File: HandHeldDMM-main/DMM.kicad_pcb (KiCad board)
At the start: 2 copper layers, 60 x 100 mm, 149 parts, among them IC1 REF35300QDBVR, J1 Conn_02x03_Odd_Even, J2 Conn_01x02, J3 Conn_01x03, J4 Conn_02x05_Odd_Even, J5 Conn_01x02, J6 Conn_01x04, J7 Conn_01x02, J8 Conn_01x01, J9 Conn_01x01, Q1 HD6362, Q10 SI2301, Q11 SI2301, Q12 SI2301, Q2 HD6362, Q3 SI2302, Q4 SI2302, Q5 SI2302, Q6 SI2301, Q7 SI2301, Q8 HD6362, Q9 SI2301, SW1 SW_Push, SW2 SW_Push, SW3 SW_Push, SW4 SW_Push, U1 TLP291, U10 TLP291, U11 LM334M, U15 CPC1017N, U17 TLP291, U18 TLP291, U19 TLP291, U20 TLP291, U21 TLP291, U22 CPC1017N, U23 CPC1017N, U24 AMS1117-5.0, U26 TL7660CDR, U27 TL7660CDR, U28 TL7660CDR, U29 CPC1017N, U3 TLP291, U30 CPC1017N, U31 CPC1017N, U4 TLP291, U5 OPA2140, U6 TLP291, U7 STM32F373CCTx, U8 AMS1117-3.3, U9 TLP291, Y1 16Mhz

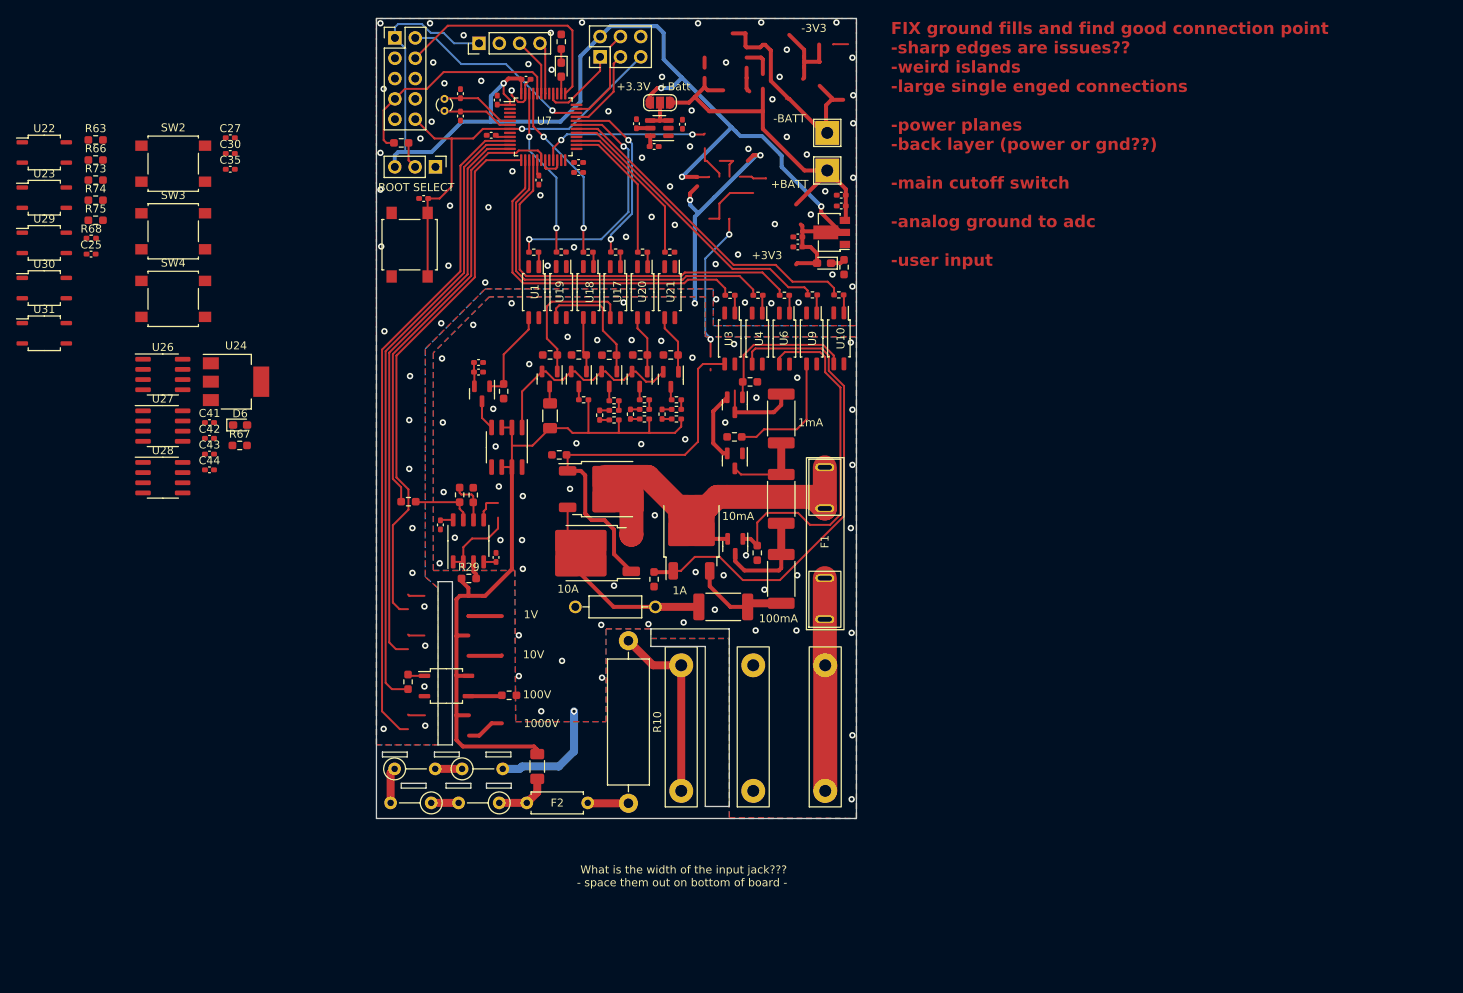
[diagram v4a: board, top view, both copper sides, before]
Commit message: Layout / routing V2 with schematic fixes
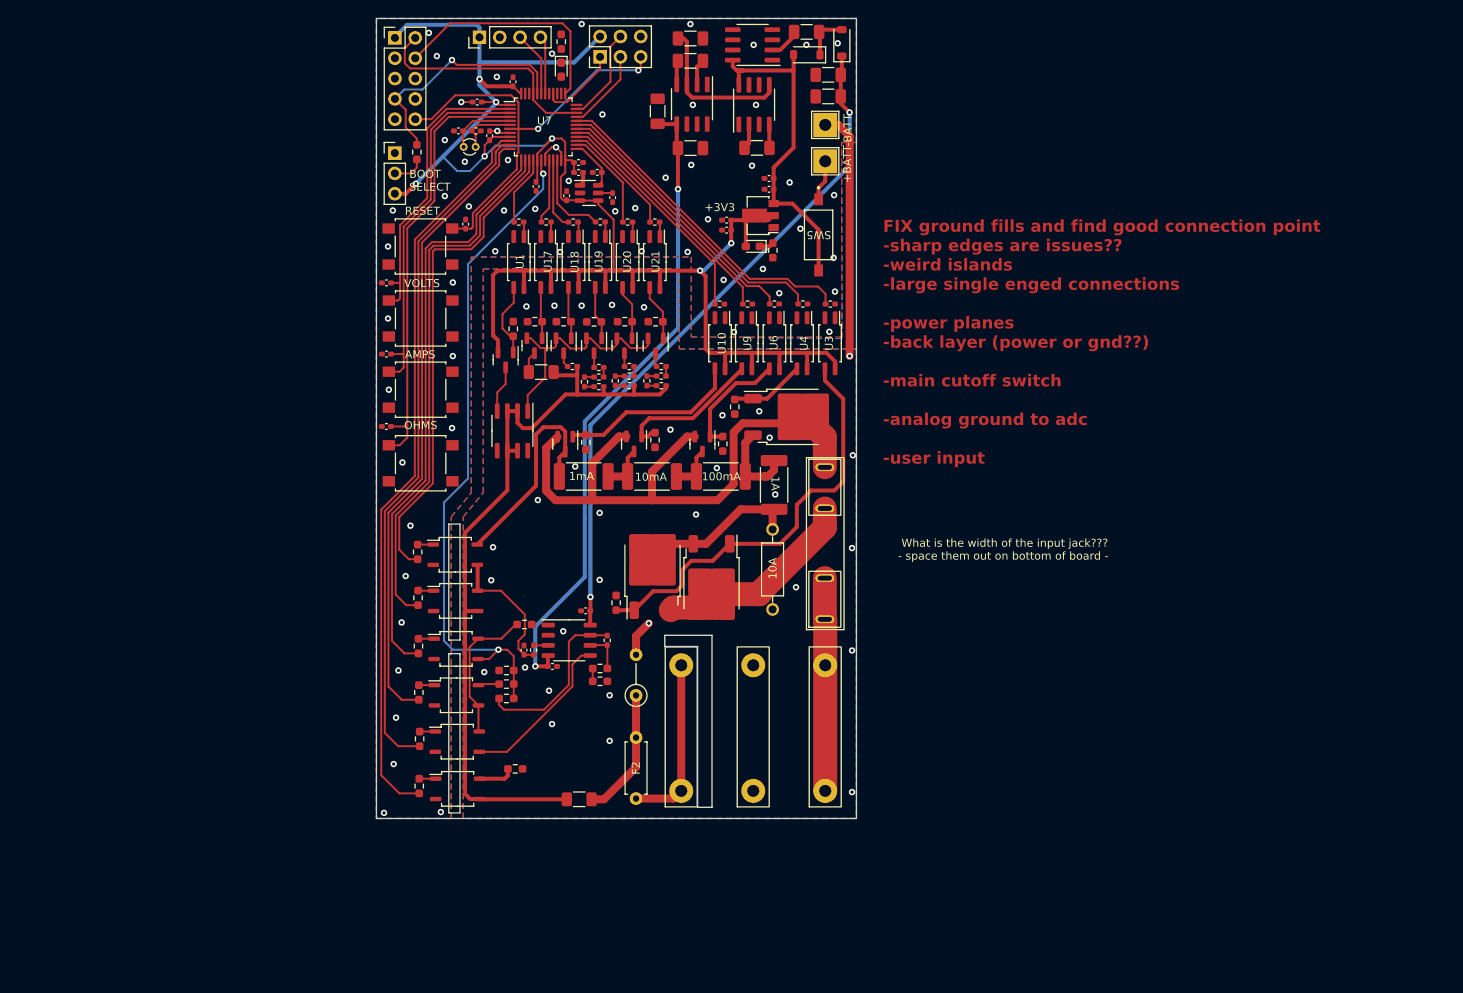
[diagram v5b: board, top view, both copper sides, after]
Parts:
- removed C41, C44: 1uF, Capacitor_SMD:C_0402_1005Metric_Pad0.74x0.62mm_HandSolder
- removed C42, C43: 100nF, Capacitor_SMD:C_0402_1005Metric_Pad0.74x0.62mm_HandSolder
- removed D6: LED, LED_SMD:LED_0603_1608Metric_Pad1.05x0.95mm_HandSolder
- removed JP1: Jumper_3_Open, Jumper:SolderJumper-3_P1.3mm_Open_RoundedPad1.0x1.5mm_NumberLabels
- removed R10: 1K, Resistor_THT:R_Axial_DIN0516_L15.5mm_D5.0mm_P20.32mm_Horizontal
- removed R67: 1k, Resistor_SMD:R_0603_1608Metric_Pad0.98x0.95mm_HandSolder
- removed RV2, RV3, RV4: Varistor, Resistor_THT:R_Axial_DIN0207_L6.3mm_D2.5mm_P5.08mm_Vertical
- removed U24: AMS1117-5.0, Package_TO_SOT_SMD:SOT-223-3_TabPin2
- added C13: 10uF, Capacitor_SMD:C_1206_3216Metric_Pad1.33x1.80mm_HandSolder, F.Cu at (168.3, 39.3)
- added C14: 10uF, Capacitor_SMD:C_1206_3216Metric_Pad1.33x1.80mm_HandSolder, F.Cu at (172.4, 33.0)
- added C15: DNP, Capacitor_SMD:C_1206_3216Metric_Pad1.33x1.80mm_HandSolder, F.Cu at (172.4, 43.9)
- added C17: 10uF, Capacitor_SMD:C_1206_3216Metric_Pad1.33x1.80mm_HandSolder, F.Cu at (172.4, 30.2)
- added C38: 10uF, Capacitor_SMD:C_1206_3216Metric_Pad1.33x1.80mm_HandSolder, F.Cu at (186.9, 29.4)
- added C40: DNP, Capacitor_SMD:C_1206_3216Metric_Pad1.33x1.80mm_HandSolder, F.Cu at (189.6, 37.4)
- added D1: 1N4148W, Diode_SMD:D_SOD-123, F.Cu at (191.3, 30.7)
- added D4: 1N4148W, Diode_SMD:D_SOD-123, F.Cu at (186.9, 32.2)
- added R1: 1K, Resistor_SMD:R_0603_1608Metric_Pad0.98x0.95mm_HandSolder, F.Cu at (161.1, 110.5)
- added R69: 4K, Resistor_SMD:R_0603_1608Metric_Pad0.98x0.95mm_HandSolder, F.Cu at (149.4, 110.9)
- added R70: 1K, Resistor_SMD:R_0603_1608Metric_Pad0.98x0.95mm_HandSolder, F.Cu at (149.4, 109.2)
- added SW5: SW_SPST, Custom Lib:Dip Switch, F.Cu at (188.4, 54.2)
- C11: value 100nF -> 10uF; footprint Capacitor_SMD:C_0402_1005Metric_Pad0.74x0.62mm_HandSolder -> Capacitor_SMD:C_1206_3216Metric_Pad1.33x1.80mm_HandSolder
- C12: value 1uF -> 10uF; footprint Capacitor_SMD:C_0402_1005Metric_Pad0.74x0.62mm_HandSolder -> Capacitor_SMD:C_1206_3216Metric_Pad1.33x1.80mm_HandSolder
- R15: value 10K -> 1K
- R16: value 145K -> 18K; footprint Resistor_SMD:R_0603_1608Metric_Pad0.98x0.95mm_HandSolder -> Resistor_SMD:R_0402_1005Metric_Pad0.72x0.64mm_HandSolder
- R30, R9: value 1k -> 1K
- moved U28 91.4 mm to (180.2, 31.0), turned to 180 degrees
- moved U27 84.1 mm to (180.4, 38.5), turned to 90 degrees
- moved R75 76.4 mm to (138.6, 117.8), turned to 90 degrees
- moved U22 76.1 mm to (143.1, 100.5)
- moved R68 75.6 mm to (152.8, 106.7), turned to 90 degrees
- moved U26 74.3 mm to (172.6, 38.4), turned to -90 degrees
- moved R74 73.6 mm to (138.4, 112.0), turned to 90 degrees
- moved C25 73.3 mm to (151.6, 106.7), turned to 90 degrees
- moved U31 72.6 mm to (143.2, 118.1)
- moved U30 72.4 mm to (143.2, 112.3)
- moved U29 72.3 mm to (143.1, 106.5)
- moved R73 70.9 mm to (138.4, 106.2), turned to 90 degrees
- moved R63 70.0 mm to (138.3, 100.1), turned to 90 degrees
- moved U23 68.0 mm to (143.0, 94.7)
- moved R66 63.4 mm to (138.3, 94.4), turned to 90 degrees
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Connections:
- net GPIO_14 renamed OOpto5
- net GPIO_15 renamed OOpto6
- net GPIO_8 renamed AOpto4
- net RButton renamed OButton
- C11 pad 1: +3.3V -> Net-(U27-CAP-)
- C11 pad 2: GNDA -> Net-(U27-CAP+)
- C12 pad 1: +3.3V -> GND
- C12 pad 2: GNDA -> OpAmpSupply+
- C25 pad 2: GNDA -> GND
- C6 pad 2: GNDA -> GND
- C7 pad 1: GNDA -> GND
- C8 pad 1: Net-(IC1-EN) -> +3.3V
- F2 pad 1: Net-(F2-Pad1) -> InputPosRaw
- IC1 pad 3: Net-(IC1-EN) -> +3.3V
- IC1 pad 4: Net-(IC1-EN) -> +3.3V
- J5 pad 1: GNDA -> GND
- J5 pad 2: GNDA -> GND
- J8 pad 1: +9V -> Net-(J8-Pin_1)
- R11 pad 1: GPIO_10 -> OOpto1
- R15 pad 1: GNDA -> Net-(R1-Pad2)
- R2 pad 2: GNDA -> GND
- R20 pad 1: GNDA -> GND
- R21 pad 2: GNDA -> GND
- R25 pad 1: GPIO_2 -> VOpto1
- R31 pad 2: GNDA -> GND
- R33 pad 2: GNDA -> GND
- R34 pad 2: GNDA -> GND
- R35 pad 2: GNDA -> GND
- R4 pad 1: GPIO_5 -> AOpto1
- R5 pad 2: GPIO_6 -> AOpto2
- R50 pad 1: GNDA -> GND
- R51 pad 1: GNDA -> GND
- R52 pad 2: GPIO_11 -> OOpto2
- R53 pad 1: GNDA -> GND
- R54 pad 2: GNDA -> GND
- R55 pad 2: GPIO_12 -> OOpto3
- R56 pad 1: GNDA -> GND
- R58 pad 2: GPIO_13 -> OOpto4
- R59 pad 1: GNDA -> GND
- R6 pad 2: GPIO_7 -> AOpto3
- R63 pad 1: GPIO_3 -> ADCOpto2
- R66 pad 1: GPIO_4 -> ADCOpto1
- R73 pad 1: GPIO_5 -> ADCOpto3
- R74 pad 1: GPIO_4 -> ADCOpto4
- R75 pad 1: GPIO_4 -> ADCOpto5
- R8 pad 2: GPIO_9 -> AOpto5
- RV1 pad 2: Net-(RV1-Pad2) -> GND
- U15 pad 3: Net-(R54-Pad1) -> InputPos
- U15 pad 4: InputPos -> Net-(R54-Pad1)
- U22 pad 3: OpAmpIn -> InputPos
- U22 pad 4: InputPos -> OpAmpIn
- U23 pad 3: CurrentOut -> OpAmpIn
- U23 pad 4: OpAmpIn -> CurrentOut
- U28 pad 8: Net-(D4-A) -> +9V
- U30 pad 3: Net-(R69-Pad1) -> BufferOut
- U30 pad 4: BufferOut -> Net-(R69-Pad1)
- U7 pad 10: GPIO_1 -> VOpto1
- U7 pad 11: GPIO_2 -> ADCOpto5
- U7 pad 12: GPIO_3 -> ADCOpto4
- U7 pad 13: GPIO_4 -> ADCOpto3
- U7 pad 14: GPIO_5 -> ADCOpto2
- U7 pad 15: GPIO_6 -> ADCOpto1
- U7 pad 16: GPIO_7 -> OOpto1
- U7 pad 19: GNDA -> GND
- U7 pad 20: unconnected-(U7-PB2-Pad20) -> OOpto2
- U7 pad 21: SD-ADC2 -> OOpto3
- U7 pad 22: GNDA -> OOpto4
- U7 pad 28: unconnected-(U7-PD8-Pad28) -> AOpto5
- U7 pad 30: GPIO_9 -> AOpto3
- U7 pad 31: GPIO_10 -> AOpto2
- U7 pad 32: GPIO_11 -> AOpto1
- U7 pad 39: GPIO_17 -> unconnected-(U7-PB3-Pad39)
- U7 pad 41: GPIO_16 -> unconnected-(U7-PB5-Pad41)
- U7 pad 45: GPIO_12 -> SWDIOPassThrough
- U7 pad 46: GPIO_13 -> unconnected-(U7-PB9-Pad46)
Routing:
- net VOpto1: track 0.00 -> 92.3 mm
- net ADCOpto5: track 0.00 -> 85.8 mm
- net GPIO_1: track 83.9 -> 0.00 mm
- net OpAmpSupply+: track 1.62 -> 85.1 mm, vias 0 -> 2
- net OpAmpSupply-: track 1.55 -> 80.6 mm, vias 0 -> 2
- net (no net): track 78.8 -> 0.00 mm, vias 2 -> 0
- net GPIO_2: track 78.5 -> 0.00 mm
- net ADCOpto4: track 0.00 -> 78.4 mm
- net ADCOpto3: track 0.00 -> 73.4 mm
- net GPIO_3: track 72.3 -> 0.00 mm
- net GPIO_4: track 68.0 -> 0.00 mm
- net ADCOpto2: track 0.00 -> 67.0 mm
- net ADCOpto1: track 0.00 -> 60.9 mm
- net +3.3V: track 164.0 -> 223.4 mm, vias 4 -> 7
- net OButton: track 0.00 -> 54.6 mm
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- removed copper zone on B.Cu, net GNDA
- removed copper zone on F.Cu, net GNDA
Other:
- outline, holes or cut-outs redrawn
- board text added: "AMPS"
- board text added: "OHMS"
- board text added: "RESET"
- board text added: "VOLTS"
- board text removed: "+3.3V"
- board text removed: "+Batt"
- board text removed: "-3V3"
- board text removed: "1000V"
- board text removed: "100V"
- board text removed: "10V"
- board text removed: "1V"

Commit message: Finished?
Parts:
- moved C26 14.7 mm to (149.0, 35.6), turned to 90 degrees
- moved R56 1.79 mm to (165.8, 64.8), turned to -90 degrees
- moved R53 1.75 mm to (161.9, 64.8), turned to -90 degrees
- moved R59 1.71 mm to (169.5, 64.7), turned to -90 degrees
- moved R51 1.56 mm to (157.9, 64.8), turned to -90 degrees
- moved C25 1.15 mm to (151.7, 107.8), turned to -90 degrees
- moved IC1 0.40 mm to (159.8, 49.9)
- moved C8 0.40 mm to (157.0, 50.2)
- moved C10 0.31 mm to (162.7, 50.4)
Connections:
- U7 pad 45: SWDIOPassThrough -> SWDIO
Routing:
- net GND: track 45.9 -> 65.3 mm, vias 91 -> 99
- net InputAmps: track 96.4 -> 101.6 mm
- net Net-(Q1-G): track 52.9 -> 49.5 mm, vias 0 -> 2
- net Net-(U5A--): track 0.00 -> 3.36 mm
- net GPIO_LED: track 0.00 -> 2.11 mm
- net Net-(R5-Pad1): track 0.00 -> 1.75 mm
- net Net-(R6-Pad1): track 0.00 -> 1.74 mm
- net Net-(R7-Pad1): track 0.00 -> 1.74 mm
- net Net-(R8-Pad1): track 0.00 -> 1.74 mm
- net Net-(R4-Pad2): track 0.00 -> 1.71 mm
- net Net-(D3-K): track 0.00 -> 1.71 mm
- net +3.3V: track 223.4 -> 221.9 mm
- net Net-(Q12-G): track 7.06 -> 8.29 mm
- net Net-(Q10-G): track 6.84 -> 7.82 mm
- net Net-(Q9-G): track 6.67 -> 7.63 mm
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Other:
- board text removed: "FIX ground fills and find good connection point -sharp edges are issues?? -weird islands -large single enged connections -power planes -back layer (power or gnd??) -main cutoff switch -analog ground to adc -user input"
- board text removed: "What is the width of the input jack??? - space them out on bottom of board -"

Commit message: Finished
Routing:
- net OpAmpIn: track 17.2 -> 16.6 mm
- net BufferOut: track 18.2 -> 18.7 mm
- net GND: vias 99 -> 100
